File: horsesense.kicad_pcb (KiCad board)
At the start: 4 copper layers, 30 x 60 mm, 73 parts, among them J1 USB4105-GF-A-120, J2 S2B-PH-SM4-TB, J3 73412-0110, J4 Conn_01x04, SW1 EVQ-P7A01P, SW2 EVQ-P7A01P, U1 MAX86141ENP+T, U2 TXB0304RUTR, U3 BQ25601, U4 XC6210B332MR, U5 XC6210B182MR, U6 LC76GPAMD, U7 AP22804AW5-7, U8 MX25L3233FM2, U9 ESP32-S3-WROOM-1-N16R8

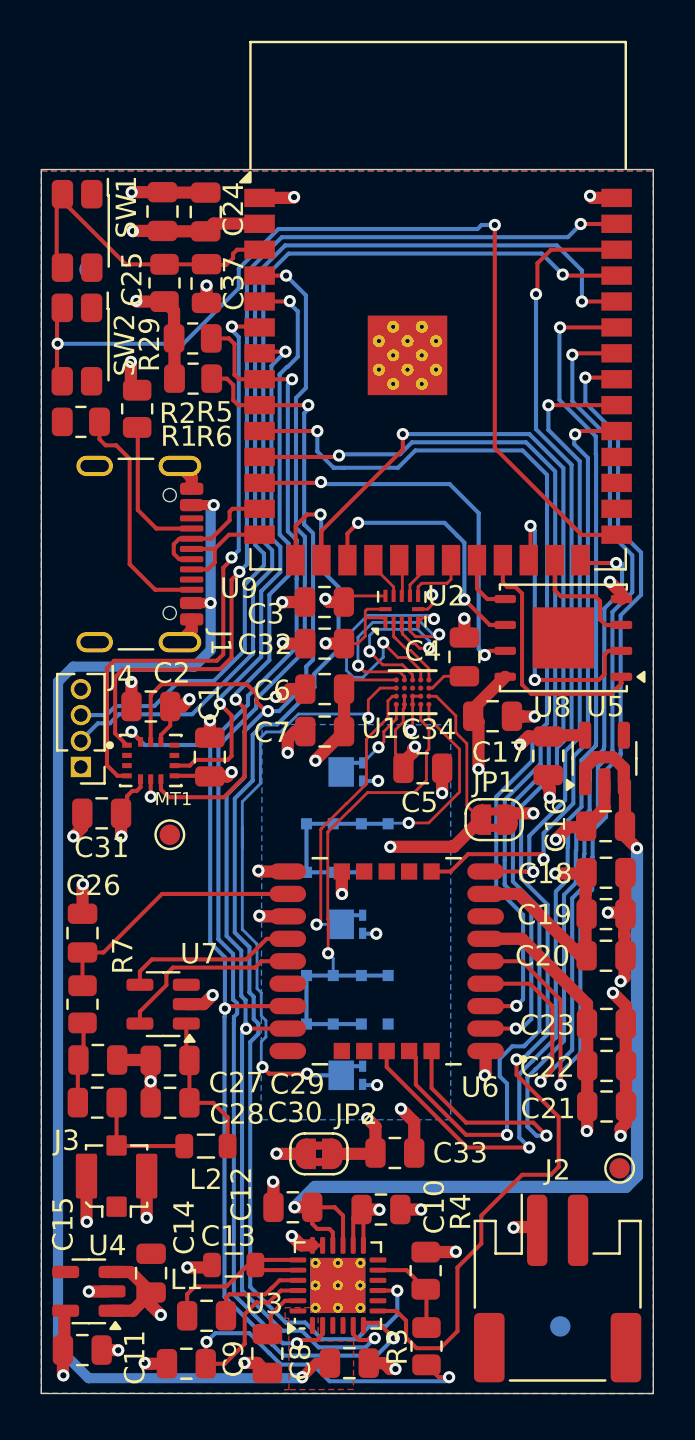
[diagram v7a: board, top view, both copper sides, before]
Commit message: Change GNSS device
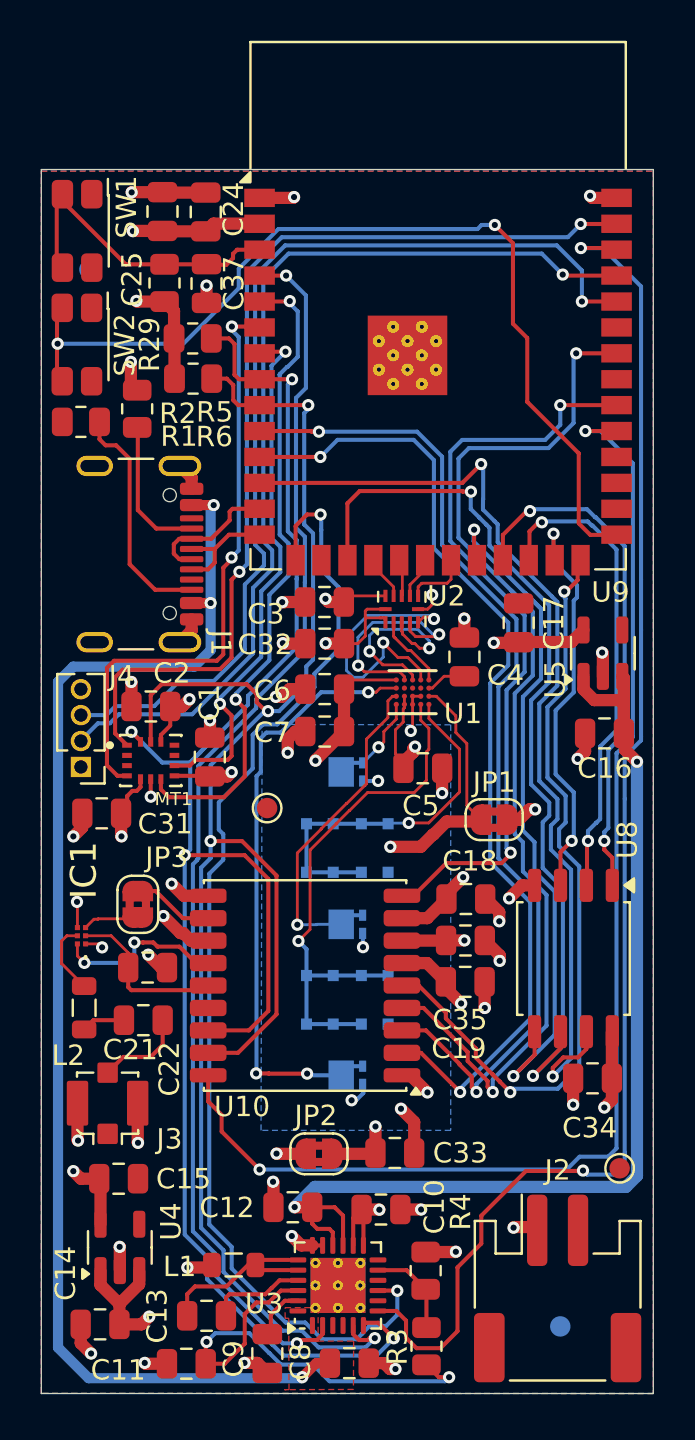
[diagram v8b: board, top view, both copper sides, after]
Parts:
- removed C20: 33p, Capacitor_SMD:C_0805_2012Metric
- removed C23, C30: 100n, Capacitor_SMD:C_0805_2012Metric
- removed C26, C27: NC, Capacitor_SMD:C_0805_2012Metric
- removed C28, C29: 100p, Capacitor_SMD:C_0805_2012Metric
- removed R7: 0, Resistor_SMD:R_0805_2012Metric
- removed U6: LC76GPAMD, Local:XCVR_LC76G
- removed U7: AP22804AW5-7, Package_TO_SOT_SMD:SOT-23-5
- added C35: 100n, Capacitor_SMD:C_0805_2012Metric, F.Cu at (160.5, 121.8)
- added IC1: BGA824N6E6329XTSA1, Local:BGA824N6E6329XTSA1, F.Cu at (141.7, 121.6)
- added JP3: SolderJumper_2_Bridged, Jumper:SolderJumper-2_P1.3mm_Bridged2Bar_RoundedPad1.0x1.5mm, F.Cu at (144.4, 120.0)
- added U10: MAX-M8Q, RF_GPS:ublox_MAX, F.Cu at (152.6, 124.0)
- C21: value 33p -> 100n
- C22: value 10µ -> 1n
- C31: value 10n -> 1µ
- L2: value 68nH -> 6.8n
- U8: value MX25L3233FM2 -> MX25L3233FM2I-08G; footprint Package_DFN_QFN:W-PDFN-8-1EP_6x5mm_P1.27mm_EP3x3mm -> Package_SO:SOIC-8_5.3x5.3mm_P1.27mm
- moved C21 23.5 mm to (144.9, 123.1)
- moved C22 22.8 mm to (144.7, 125.7)
- moved C34 18.4 mm to (166.7, 128.6), turned to 180 degrees
- moved U8 15.7 mm to (165.8, 122.7), turned to -90 degrees
- moved L2 9.03 mm to (141.8, 125.1), turned to -90 degrees
- moved C15 8.59 mm to (143.5, 133.5)
- moved C19 7.66 mm to (160.5, 123.8)
- moved C18 6.99 mm to (160.5, 119.8)
- moved C17 6.68 mm to (163.1, 106.2), turned to 90 degrees
- moved U5 5.16 mm to (167.2, 107.7)
- moved TP1 4.95 mm to (150.8, 115.3)
- moved C16 4.55 mm to (167.3, 111.7)
- moved J3 3.60 mm to (142.9, 129.8)
- moved C14 3.54 mm to (142.6, 140.6), turned to 180 degrees
- moved U4 2.64 mm to (143.5, 136.9), turned to 90 degrees
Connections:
- C21 pad 1: +3.3V -> Net-(IC1-VCC)
- C22 pad 1: +3.3V -> Net-(C22-Pad1)
- C22 pad 2: GND -> Net-(J3-In)
- L2 pad 1: Net-(J3-In) -> Net-(IC1-AI)
- L2 pad 2: Net-(U7-OUT) -> Net-(C22-Pad1)
- U9 pad 16: GPS_JAM -> unconnected-(U9-IO46-Pad16)
- U9 pad 33: GPS_REQ -> unconnected-(U9-IO40-Pad33)
- U9 pad 35: GPS_REF -> unconnected-(U9-IO42-Pad35)
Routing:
- net GPS_JAM: track 59.2 -> 0.00 mm, vias 2 -> 0
- net GPS_REF: track 54.9 -> 0.00 mm, vias 2 -> 0
- net GPS_REQ: track 47.6 -> 0.00 mm, vias 2 -> 0
- net FLASH_SID0: track 2.99 -> 35.3 mm, vias 0 -> 2
- net GPS_SEL: track 30.2 -> 62.0 mm
- net FLASH_SCLK: track 13.0 -> 44.0 mm
- net FLASH_SID3: track 19.6 -> 47.8 mm
- net +3.3V: track 64.9 -> 50.5 mm, vias 12 -> 13
- net FLASH_SID2: track 5.98 -> 20.1 mm, vias 0 -> 2
- net GND: track 77.2 -> 63.1 mm, vias 44 -> 42
- net SCL: track 72.9 -> 86.6 mm
- net FLASH_CS: track 12.5 -> 25.7 mm, vias 0 -> 2
- net SDA: track 72.7 -> 85.7 mm
- net Net-(U6-RF_IN): track 12.6 -> 0.00 mm
- net Net-(U6-VDD_RF): track 9.17 -> 0.00 mm
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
